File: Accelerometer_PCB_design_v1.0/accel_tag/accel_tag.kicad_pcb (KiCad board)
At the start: 2 copper layers, 80.1 x 22.5 mm, 14 parts, among them J1 Conn_01x08, U1 LIS2DU12TR, U2 DA14531-00000OG2, Y1 ABM13W-32MHz

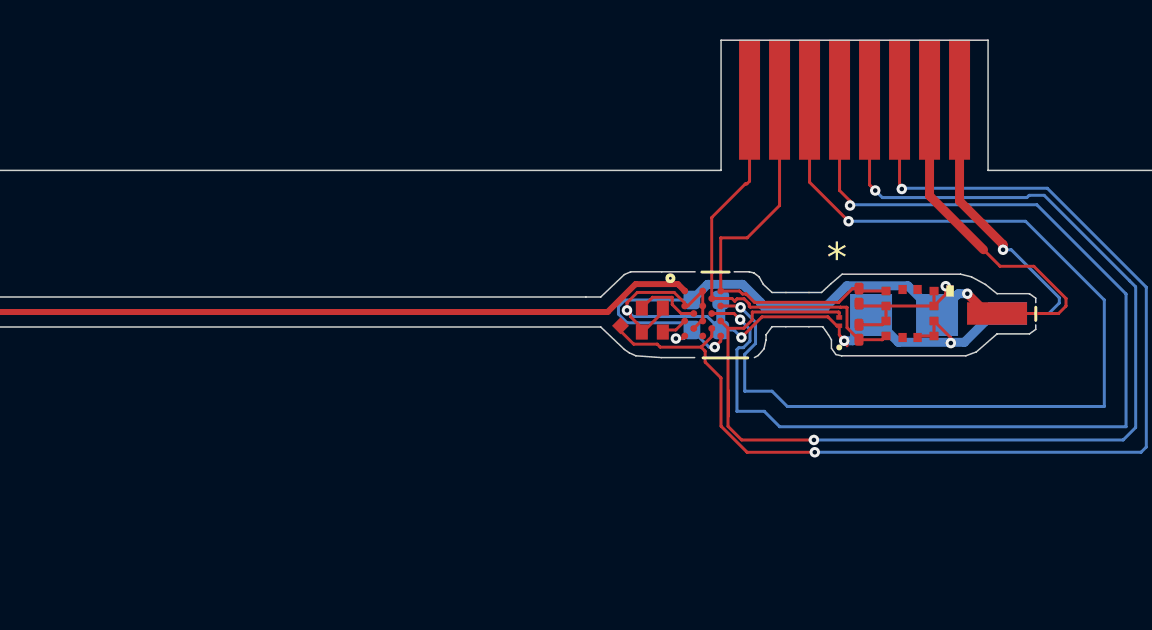
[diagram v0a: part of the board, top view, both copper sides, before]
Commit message: tweaking tracks around crystal; narrower perimeter
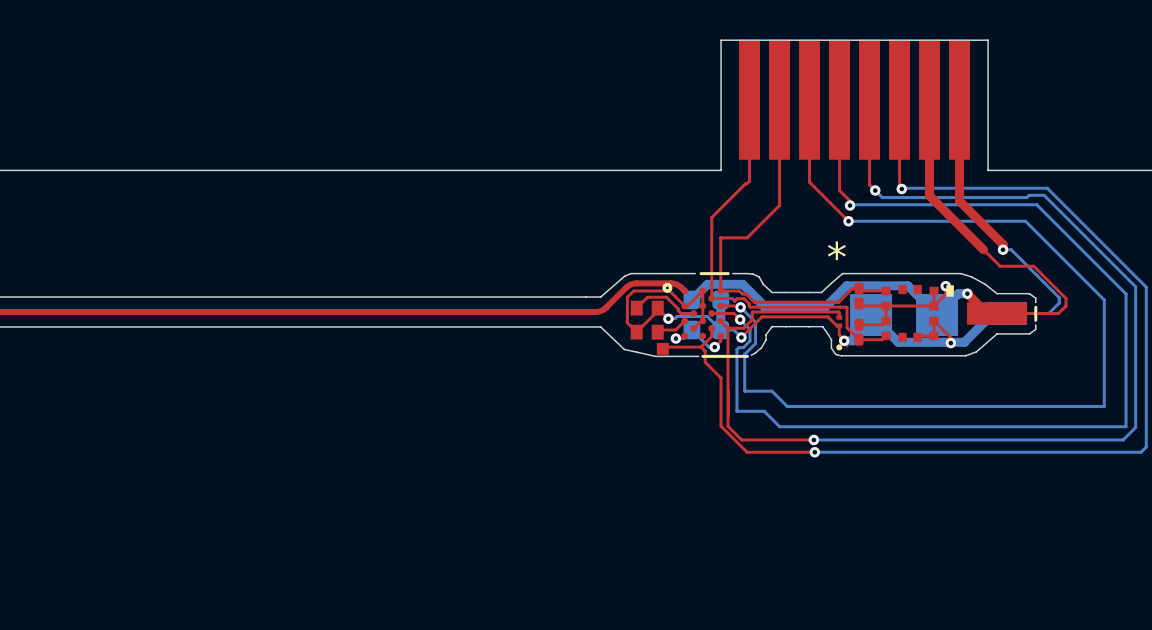
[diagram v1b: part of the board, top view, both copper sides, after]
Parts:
- moved TP1 1.61 mm to (120.2, 72.7)
- moved Y1 0.17 mm to (119.6, 71.8)
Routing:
- net Net-(J1-Pin_7): track 38.4 -> 32.9 mm
- net Net-(J1-Pin_6): track 39.2 -> 37.5 mm
- net GNDREF: track 36.2 -> 34.9 mm
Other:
- outline, holes or cut-outs redrawn

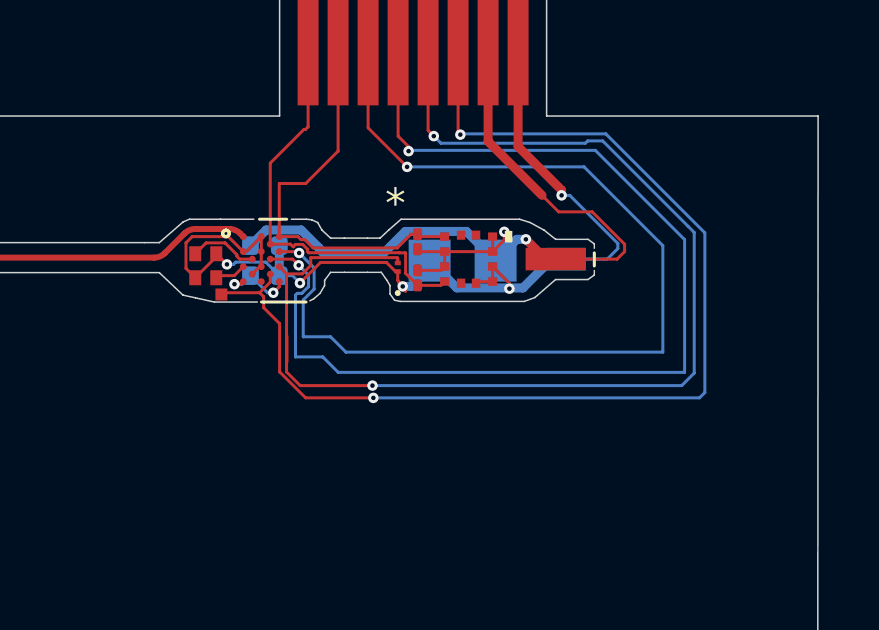
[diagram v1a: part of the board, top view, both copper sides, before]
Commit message: Added BOM, silkscreen instructions
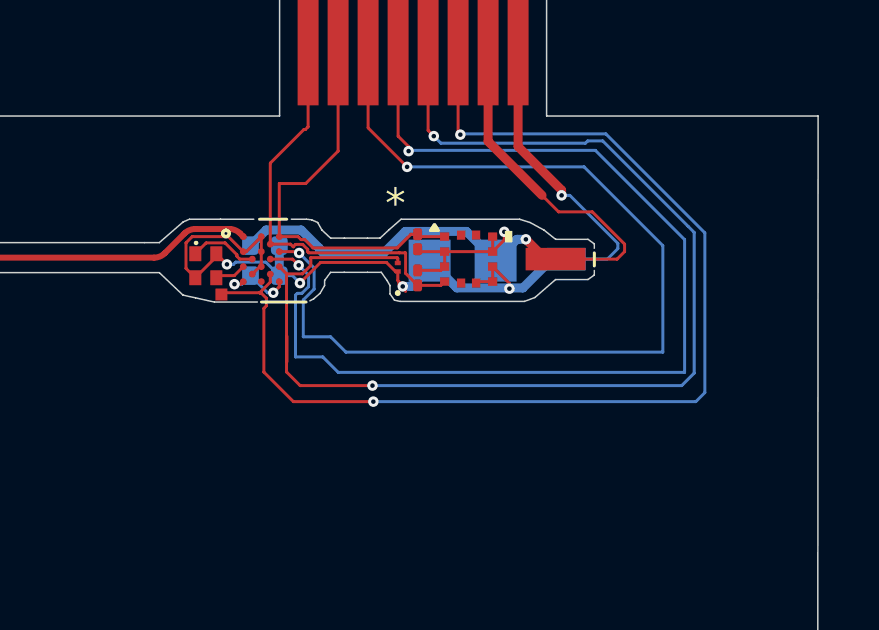
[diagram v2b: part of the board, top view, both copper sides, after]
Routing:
- net Net-(J1-Pin_6): track 37.5 -> 38.0 mm
